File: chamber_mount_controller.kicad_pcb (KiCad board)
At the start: 2 copper layers, 10 parts, among them J1 Conn_01x04, J2 Conn_01x04, J3 Conn_01x02

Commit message: updated files
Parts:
- added G***: LOGO, Library:cirno_logo, F.Cu at (91.2, 54.4)
- moved J3 3.54 mm to (125.2, 54.4)
- moved C1 0.25 mm to (138.5, 53.1)
- renumbered AZI_MS to SW1, ELE_MS to SW2, AZI to U1, ELE to U2
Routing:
- net VCC: track 39.1 -> 40.1 mm
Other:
- board outline added: 69.6 x 54.4 mm
- board text added: "00: 1/1 01: 1/2 10: 1/4 11: 1/8"
- board text added: "MARS_stepper_shield"

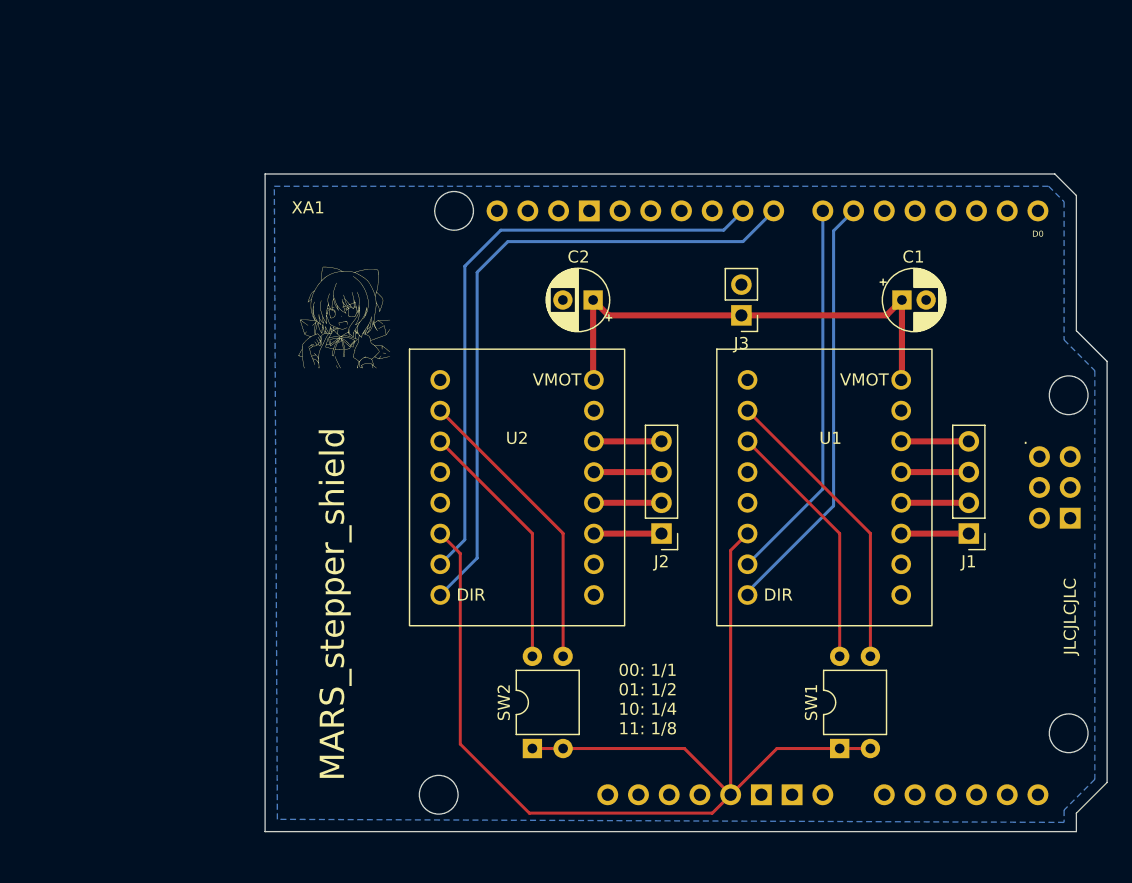
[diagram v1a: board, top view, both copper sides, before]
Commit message: Redid layout for arduino nano, added DC barrel jack
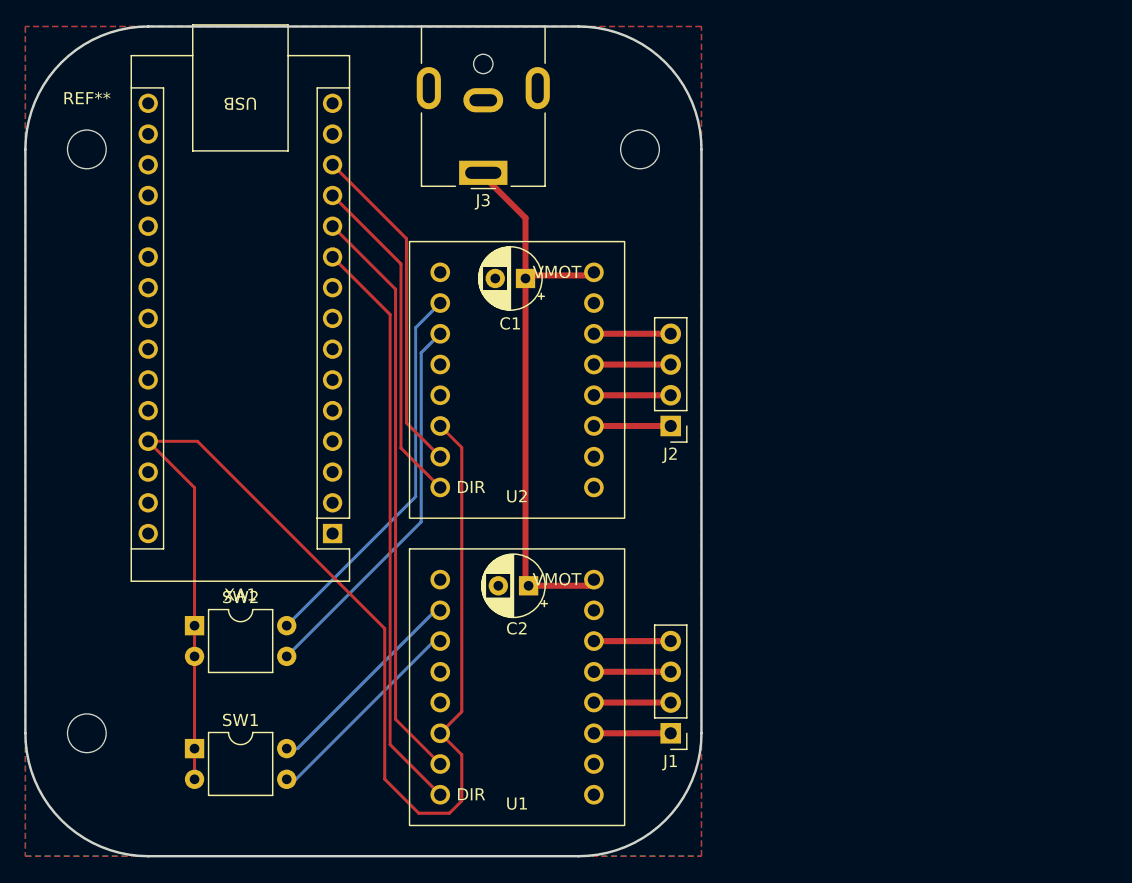
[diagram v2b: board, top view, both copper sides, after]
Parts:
- removed G***: LOGO, Library:cirno_logo
- added REF**: MountingHole_3.2mm_M3, MountingHole:MountingHole_3.2mm_M3, F.Cu at (116.8, 40.6)
- added REF**: MountingHole_3.2mm_M3, MountingHole:MountingHole_3.2mm_M3, F.Cu at (71.1, 40.6)
- added REF**: MountingHole_3.2mm_M3, MountingHole:MountingHole_3.2mm_M3, F.Cu at (71.1, 88.9)
- C1: footprint Capacitor_THT:CP_Radial_D5.0mm_P2.00mm -> Capacitor_THT:CP_Radial_D5.0mm_P2.50mm
- J3: footprint Connector_PinHeader_2.54mm:PinHeader_1x02_P2.54mm_Vertical -> Connector_BarrelJack:BarrelJack_CUI_PJ-063AH_Horizontal
- XA1: footprint Arduino:Arduino_Uno_Shield -> Module:Arduino_Nano
- moved SW1 53.3 mm to (80.0, 90.2), turned to 0 degrees
- moved C1 31.2 mm to (107.4, 51.3), turned to 180 degrees
- moved U1 30.3 mm to (100.3, 76.2)
- moved SW2 29.7 mm to (80.0, 80.0), turned to 0 degrees
- moved J1 29.7 mm to (119.4, 88.9)
- moved XA1 24.7 mm to (91.4, 72.4), turned to 180 degrees
- moved J3 24.4 mm to (103.9, 42.6)
- moved C2 24.2 mm to (107.6, 76.7)
- moved J2 8.92 mm to (119.4, 63.5)
- moved U2 8.89 mm to (100.3, 50.8)
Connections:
- SW1 pad 3: Net-(SW1-Pad3) -> Net-(U1-ms2)
- SW1 pad 4: Net-(SW1-Pad4) -> Net-(U1-ms1)
- SW2 pad 3: Net-(SW2-Pad3) -> Net-(U2-ms2)
- SW2 pad 4: Net-(SW2-Pad4) -> Net-(U2-ms1)
- U1 pad 2: Net-(SW1-Pad3) -> Net-(U1-ms1)
- U1 pad 3: Net-(SW1-Pad4) -> Net-(U1-ms2)
- U1 pad 7: Net-(U1-Pad7) -> Net-(U1-step)
- U1 pad 8: Net-(U1-Pad8) -> Net-(U1-dir)
- U2 pad 2: Net-(SW2-Pad3) -> Net-(U2-ms1)
- U2 pad 3: Net-(SW2-Pad4) -> Net-(U2-ms2)
- U2 pad 7: Net-(U2-Pad7) -> Net-(U2-step)
- U2 pad 8: Net-(U2-Pad8) -> Net-(U2-dir)
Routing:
- net Net-(U2-Pad8): track 54.5 -> 0.00 mm
- net Net-(U2-Pad7): track 50.4 -> 0.00 mm
- net Net-(U1-step): track 0.00 -> 48.1 mm
- net Net-(U1-dir): track 0.00 -> 48.1 mm
- net Net-(U1-Pad8): track 35.4 -> 0.00 mm
- net Net-(U2-ms2): track 0.00 -> 31.9 mm
- net Net-(U2-ms1): track 0.00 -> 31.9 mm
- net Net-(U1-Pad7): track 31.8 -> 0.00 mm
- net Net-(U2-step): track 0.00 -> 27.8 mm
- net Net-(U2-dir): track 0.00 -> 27.8 mm
- net Net-(SW2-Pad3): track 24.5 -> 0.00 mm
- net Net-(SW1-Pad3): track 24.5 -> 0.00 mm
- net Net-(SW2-Pad4): track 20.9 -> 0.00 mm
- net Net-(SW1-Pad4): track 20.9 -> 0.00 mm
- net Net-(U1-ms1): track 0.00 -> 17.4 mm
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- added copper zone on F.Cu, net GND
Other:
- board size 69.6 x 54.4 mm -> 55.9 x 68.6 mm
- board text removed: "00: 1/1 01: 1/2 10: 1/4 11: 1/8"
- board text removed: "JLCJLCJLC"
- board text removed: "MARS_stepper_shield"

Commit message: Re-routed traces to remove need for microstepping DIP switches
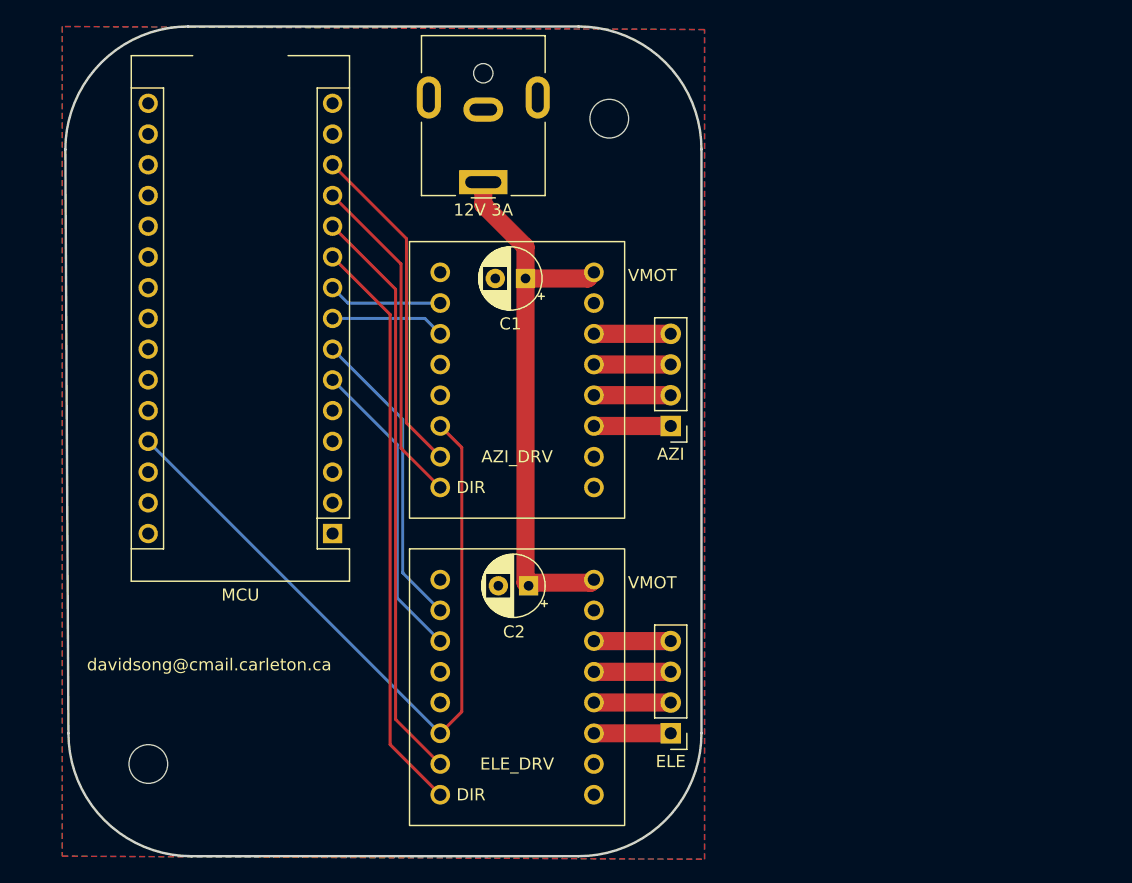
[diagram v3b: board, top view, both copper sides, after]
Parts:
- removed the REF** at (116.8, 40.6)
- removed the REF** at (71.1, 40.6)
- removed the REF** at (71.1, 88.9)
- removed SW1, SW2: SW_DIP_x02, Package_DIP:DIP-4_W7.62mm
- added G***: LOGO, misc_silkscreen:logo, F.Cu at (88.9, 88.9)
- added REF**: MountingHole_3.2mm_M3, MountingHole:MountingHole_3.2mm_M3, F.Cu at (76.2, 91.4)
- added REF**: MountingHole_3.2mm_M3, MountingHole:MountingHole_3.2mm_M3, F.Cu at (114.3, 38.1)
- 12V 3A: renamed from J3
- moved 12V 3A 0.77 mm to (103.9, 43.3)
- renumbered J2 to AZI, U2 to AZI_DRV, J1 to ELE, U1 to ELE_DRV, XA1 to MCU
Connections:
- MCU pad 6: unconnected-(XA1-D3-Pad6) -> Net-(U1-ms2)
- MCU pad 7: unconnected-(XA1-D4-Pad7) -> Net-(U1-ms1)
- MCU pad 8: unconnected-(XA1-D5-Pad8) -> Net-(U2-ms2)
- MCU pad 9: unconnected-(XA1-D6-Pad9) -> Net-(U2-ms1)
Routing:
- net +5V: track 109.1 -> 61.0 mm
- net Net-(U2-ms2): track 31.9 -> 9.43 mm
- net Net-(U2-ms1): track 31.9 -> 9.43 mm
- net Net-(U1-ms2): track 17.4 -> 25.3 mm
- net Net-(U1-ms1): track 17.4 -> 25.3 mm
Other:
- board size 55.9 x 68.6 mm -> 52.6 x 68.6 mm
- board text added: "MARS_2axis_system"
- board text added: "davidsong@cmail.carleton.ca"
